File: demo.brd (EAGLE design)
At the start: 12.7 x 14 mm, 4 parts

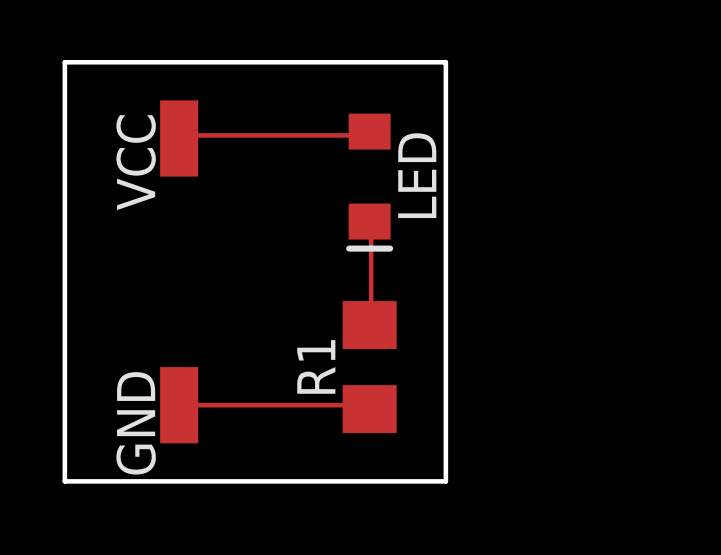
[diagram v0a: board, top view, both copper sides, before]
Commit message: Added custom part
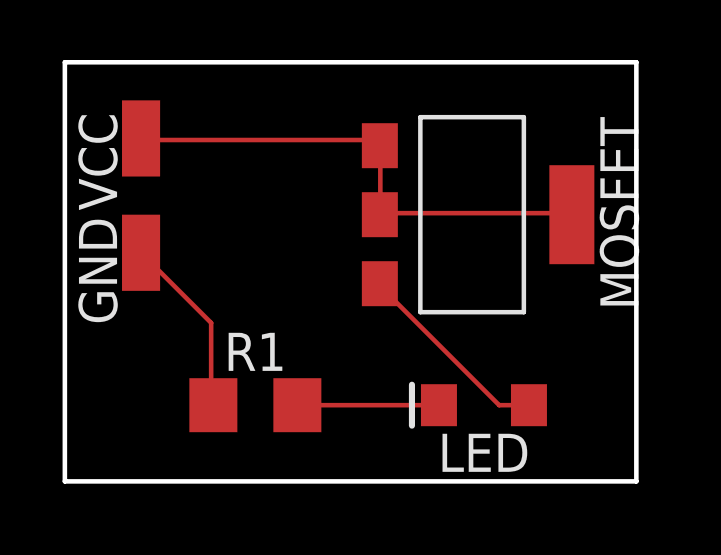
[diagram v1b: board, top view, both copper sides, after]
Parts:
- added MOSFET: ???, mylib:CSTM_MOSFET
- moved LED 8.52 mm to (14.0, 3.81), turned to 180 degrees
- moved GND 5.24 mm to (2.54, 8.89)
- moved R1 4.02 mm to (6.35, 3.81), turned to 0 degrees
- moved VCC 1.27 mm to (2.54, 12.7)
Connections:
- removed net N$1 (its old number): LED.A, VCC.1
- new net N$3: MOSFET.1, MOSFET.2, MOSFET.2B, VCC.1
- new net N$4: LED.A, MOSFET.3
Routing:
- net N$3: track 0.00 -> 16.7 mm
- net N$4: track 0.00 -> 6.68 mm
- net N$1 (its old number): track 6.51 -> 0.00 mm
- net N$2: track 3.50 -> 4.72 mm
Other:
- board size 12.7 x 14 mm -> 19.1 x 14 mm
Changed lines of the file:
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@@
 <drawing>
 <settings>
-<setting alwaysvectorfont="yes"/>
+<setting alwaysvectorfont="no"/>
 <setting verticaltext="up"/>
 </settings>
@@
 <plain>
 <wire x1="0" y1="1.27" x2="0" y2="15.24" width="0.1524" layer="20"/>
-<wire x1="0" y1="15.24" x2="12.7" y2="15.24" width="0.1524" layer="20"/>
-<wire x1="12.7" y1="15.24" x2="12.7" y2="1.27" width="0.1524" layer="20"/>
-<wire x1="12.7" y1="1.27" x2="0" y2="1.27" width="0.1524" layer="20"/>
+<wire x1="0" y1="15.24" x2="19.05" y2="15.24" width="0.1524" layer="20"/>
+<wire x1="19.05" y1="15.24" x2="19.05" y2="1.27" width="0.1524" layer="20"/>
+<wire x1="19.05" y1="1.27" x2="0" y2="1.27" width="0.1524" layer="20"/>
 </plain>
 <attributes>
@@
 </autorouter>
 <elements>
-<element name="GND" library="wirepad" library_urn="urn:adsk.eagle:library:412" package="SMD1,27-2,54" package3d_urn="urn:adsk.eagle:package:30839/1" value="" x="3.81" y="3.81" smashed="yes">
-<attribute name="NAME" x="3.01" y="1.41" size="1.27" layer="25" rot="R90"/>
-<attribute name="POPULARITY" value="15" x="17.78" y="0" size="1.778" layer="27" display="off"/>
-<attribute name="VALUE" x="3.81" y="3.81" size="0.0254" layer="27"/>
+<element name="GND" library="wirepad" library_urn="urn:adsk.eagle:library:412" package="SMD1,27-2,54" package3d_urn="urn:adsk.eagle:package:30839/1" value="" x="2.54" y="8.89" smashed="yes">
+<attribute name="NAME" x="1.74" y="6.49" size="1.27" layer="25" rot="R90"/>
+<attribute name="POPULARITY" value="15" x="16.51" y="5.08" size="1.778" layer="27" display="off"/>
+<attribute name="VALUE" x="2.54" y="8.89" size="0.0254" layer="27"/>
 </element>
-<element name="LED" library="SparkFun-LED" package="LED-1206" value="RED" x="10.16" y="11.43" smashed="yes" rot="R270">
-<attribute name="NAME" x="11.1125" y="11.43" size="1.27" layer="25" font="vector" ratio="20" rot="R270" align="bottom-center"/>
-<attribute name="PROD_ID" value="DIO-09912" x="-3.81" y="-3.81" size="1.778" layer="27" rot="R270" display="off"/>
-<attribute name="VALUE" x="9.2075" y="11.43" size="1.27" layer="27" font="vector" ratio="20" rot="R270" align="top-center"/>
+<element name="LED" library="SparkFun-LED" package="LED-1206" value="RED" x="13.97" y="3.81" smashed="yes" rot="R180">
+<attribute name="NAME" x="13.97" y="2.8575" size="1.27" layer="25" font="vector" ratio="20" rot="R180" align="bottom-center"/>
+<attribute name="PROD_ID" value="DIO-09912" x="-1.27" y="17.78" size="1.778" layer="27" rot="R180" display="off"/>
+<attribute name="VALUE" x="13.97" y="4.7625" size="1.27" layer="27" font="vector" ratio="20" rot="R180" align="top-center"/>
 </element>
-<element name="R1" library="SparkFun-Resistors" package="1206" value="330" x="10.16" y="5.08" smashed="yes" rot="R90">
-<attribute name="NAME" x="9.017" y="5.08" size="1.27" layer="25" font="vector" ratio="20" rot="R90" align="bottom-center"/>
-<attribute name="PROD_ID" value=" " x="19.05" y="20.32" size="1.778" layer="27" rot="R90" display="off"/>
-<attribute name="VALUE" x="11.303" y="5.08" size="1.27" layer="27" font="vector" ratio="20" rot="R90" align="top-center"/>
+<element name="R1" library="SparkFun-Resistors" package="1206" value="330" x="6.35" y="3.81" smashed="yes">
+<attribute name="NAME" x="6.35" y="4.953" size="1.27" layer="25" font="vector" ratio="20" align="bottom-center"/>
+<attribute name="PROD_ID" value=" " x="21.59" y="-5.08" size="1.778" layer="27" display="off"/>
+<attribute name="VALUE" x="6.35" y="2.667" size="1.27" layer="27" font="vector" ratio="20" align="top-center"/>
 </element>
-<element name="VCC" library="wirepad" library_urn="urn:adsk.eagle:library:412" package="SMD1,27-2,54" package3d_urn="urn:adsk.eagle:package:30839/1" value="" x="3.81" y="12.7" smashed="yes">
-<attribute name="NAME" x="3.01" y="10.3" size="1.27" layer="25" rot="R90"/>
-<attribute name="POPULARITY" value="15" x="21.59" y="8.89" size="1.778" layer="27" display="off"/>
-<attribute name="VALUE" x="3.81" y="12.7" size="0.0254" layer="27"/>
+<element name="VCC" library="wirepad" library_urn="urn:adsk.eagle:library:412" package="SMD1,27-2,54" package3d_urn="urn:adsk.eagle:package:30839/1" value="" x="2.54" y="12.7" smashed="yes">
+<attribute name="NAME" x="1.74" y="10.3" size="1.27" layer="25" rot="R90"/>
+<attribute name="POPULARITY" value="15" x="20.32" y="8.89" size="1.778" layer="27" display="off"/>
+<attribute name="VALUE" x="2.54" y="12.7" size="0.0254" layer="27"/>
+</element>
+<element name="MOSFET" library="mylib" package="CSTM_MOSFET" value="???" x="12.7" y="10.16" smashed="yes" rot="R270">
+<attribute name="NAME" x="17.85" y="13.41" size="1.27" layer="25" rot="R270"/>
+<attribute name="VALUE" x="8.45" y="13.71" size="1.27" layer="27" rot="R270"/>
 </element>
 </elements>
 <signals>
-<signal name="N$1">
-<contactref element="VCC" pad="1"/>
-<contactref element="LED" pad="A"/>
-<wire x1="3.81" y1="12.8016" x2="10.0584" y2="12.8016" width="0.1524" layer="1"/>
-<wire x1="10.0584" y1="12.8016" x2="10.16" y2="12.93" width="0.1524" layer="1"/>
-<wire x1="3.81" y1="12.8016" x2="3.81" y2="12.7" width="0.1524" layer="1"/>
-</signal>
 <signal name="N$2">
 <contactref element="LED" pad="C"/>
 <contactref element="R1" pad="2"/>
-<wire x1="10.2108" y1="6.5532" x2="10.2108" y2="9.906" width="0.1524" layer="1"/>
-<wire x1="10.2108" y1="9.906" x2="10.16" y2="9.93" width="0.1524" layer="1"/>
-<wire x1="10.2108" y1="6.5532" x2="10.16" y2="6.48" width="0.1524" layer="1"/>
+<wire x1="7.75" y1="3.81" x2="12.47" y2="3.81" width="0.1524" layer="1"/>
+</signal>
+<signal name="N$1">
+<contactref element="R1" pad="1"/>
+<contactref element="GND" pad="1"/>
+<wire x1="2.54" y1="8.89" x2="2.55563125" y2="8.89" width="0.1524" layer="1"/>
+<wire x1="4.8768" y1="6.5532" x2="4.8768" y2="3.81" width="0.1524" layer="1"/>
+<wire x1="2.54" y1="8.89" x2="4.8768" y2="6.5532" width="0.1524" layer="1"/>
+<wire x1="4.8768" y1="3.81" x2="4.95" y2="3.81" width="0.1524" layer="1"/>
 </signal>
 <signal name="N$3">
-<contactref element="R1" pad="1"/>
-<contactref element="GND" pad="1"/>
-<wire x1="3.81" y1="3.81" x2="10.0584" y2="3.81" width="0.1524" layer="1"/>
-<wire x1="10.0584" y1="3.81" x2="10.16" y2="3.68" width="0.1524" layer="1"/>
+<contactref element="MOSFET" pad="2"/>
+<contactref element="MOSFET" pad="2B"/>
+<contactref element="VCC" pad="1"/>
+<contactref element="MOSFET" pad="1"/>
+<wire x1="10.5156" y1="12.3444" x2="10.5156" y2="10.2108" width="0.1524" layer="1"/>
+<wire x1="10.5156" y1="12.3444" x2="10.5" y2="12.46" width="0.1524" layer="1"/>
+<wire x1="16.764" y1="10.2108" x2="10.5156" y2="10.2108" width="0.1524" layer="1"/>
+<wire x1="10.5156" y1="10.2108" x2="10.5" y2="10.16" width="0.1524" layer="1"/>
+<wire x1="16.764" y1="10.2108" x2="16.9" y2="10.16" width="0.1524" layer="1"/>
+<wire x1="10.2108" y1="12.6492" x2="2.5908" y2="12.6492" width="0.1524" layer="1"/>
+<wire x1="10.3632" y1="12.4968" x2="10.2108" y2="12.6492" width="0.1524" layer="1"/>
+<wire x1="2.5908" y1="12.6492" x2="2.54" y2="12.7" width="0.1524" layer="1"/>
+<wire x1="10.3632" y1="12.4968" x2="10.5" y2="12.46" width="0.1524" layer="1"/>
+</signal>
+<signal name="N$4">
+<contactref element="MOSFET" pad="3"/>
+<contactref element="LED" pad="A"/>
+<wire x1="14.478" y1="3.81" x2="15.47" y2="3.81" width="0.1524" layer="1"/>
+<wire x1="10.5156" y1="7.7724" x2="14.478" y2="3.81" width="0.1524" layer="1"/>
+<wire x1="10.5156" y1="7.7724" x2="10.5" y2="7.86" width="0.1524" layer="1"/>
 </signal>
 </signals>
